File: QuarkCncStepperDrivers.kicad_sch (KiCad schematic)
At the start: 2 parts, among them J1 Conn_01x14, J2 Conn_01x14

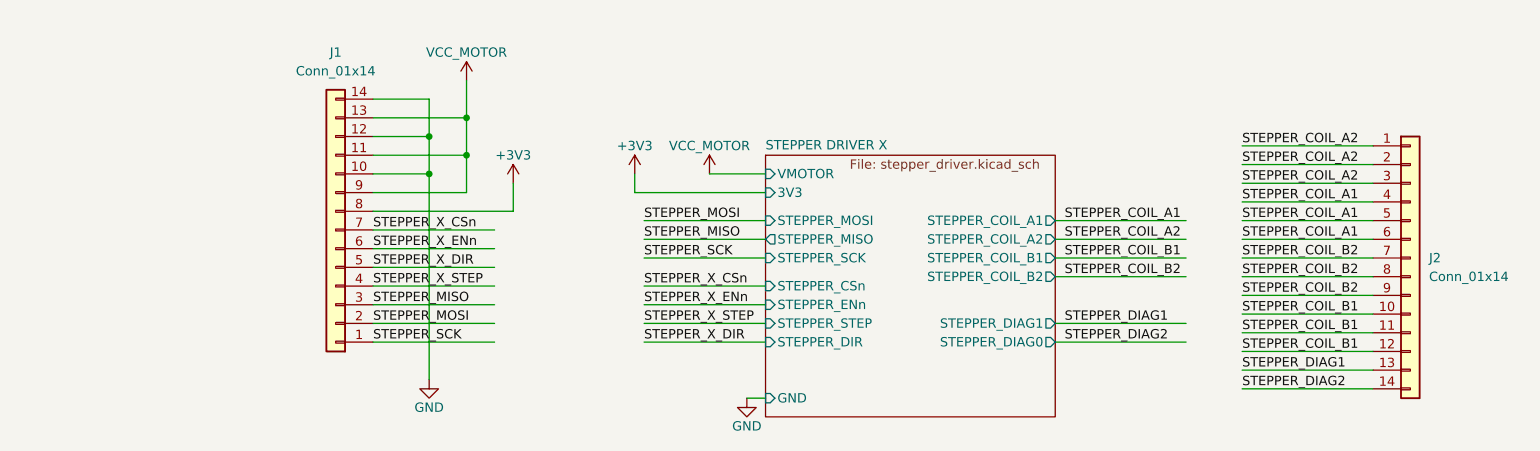
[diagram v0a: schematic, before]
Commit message: Removed caps from board. Will be placed on main board
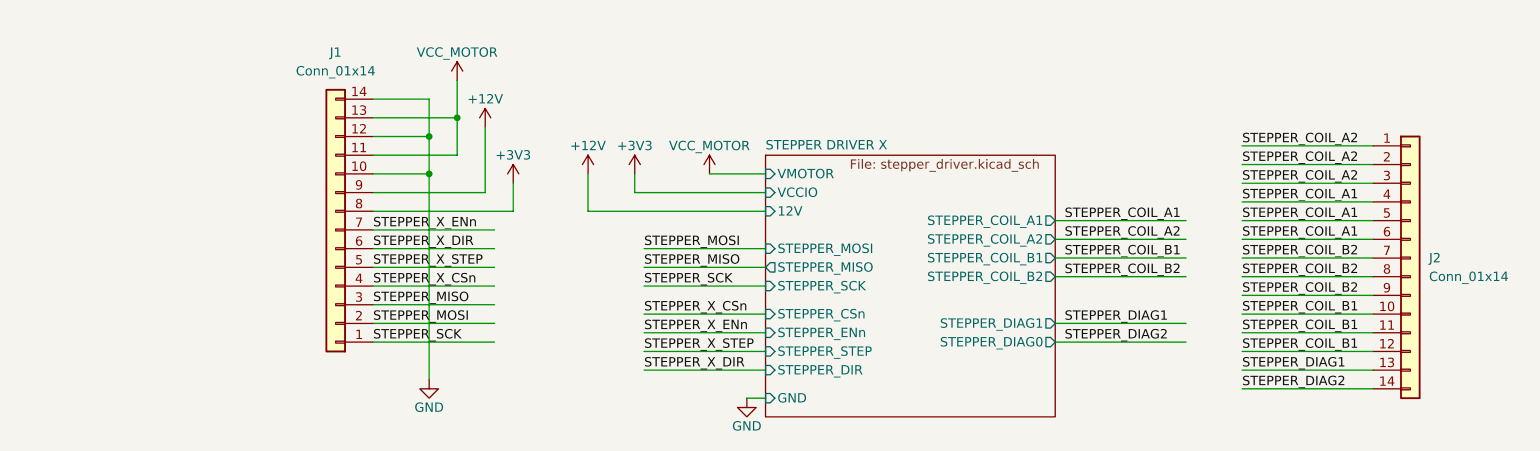
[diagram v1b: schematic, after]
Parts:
- J1, J2: LCSC (none) -> C2894937
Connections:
- net STEPPER_X_CSn: now also J1.4 (Pin_4); no longer J1.7 (Pin_7)
- net STEPPER_X_DIR: now also J1.6 (Pin_6); no longer J1.5 (Pin_5)
- net STEPPER_X_ENn: now also J1.7 (Pin_7); no longer J1.6 (Pin_6)
- net STEPPER_X_STEP: now also J1.5 (Pin_5); no longer J1.4 (Pin_4)
- net VCC: no longer J1.9 (Pin_9)
- new net +12V: J1.9 (Pin_9)
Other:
- sheet STEPPER DRIVER X ports: added 12V, VCCIO; removed 3V3

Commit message: triple connector
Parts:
- removed J1: Conn_01x14, Connector_PinHeader_2.54mm:PinHeader_1x14_P2.54mm_Vertical, symbol Connector_Generic:Conn_01x14
- added J1: (no value), symbol Connector_Generic:Conn_02x03_Odd_Even
- added J2: Conn_01x08, Connector_PinSocket_2.54mm:PinSocket_1x08_P2.54mm_Vertical, symbol Connector_Generic:Conn_01x08
- renumbered J2 to J3
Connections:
- net +12V: now also J1.2 (Pin_2)
- net +3V3: now also J1.1 (Pin_1)
- net GND: now also J1.3 (Pin_3), J1.4 (Pin_4), J2.5 (Pin_5)
- net STEPPER_MISO: now also J2.3 (Pin_3)
- net STEPPER_MOSI: now also J2.2 (Pin_2)
- net STEPPER_SCK: now also J2.1 (Pin_1)
- net STEPPER_X_CSn: now also J2.4 (Pin_4)
- net STEPPER_X_DIR: now also J2.7 (Pin_7)
- net STEPPER_X_ENn: now also J2.8 (Pin_8)
- net STEPPER_X_STEP: now also J2.6 (Pin_6)
- net VCC: now also J1.5 (Pin_5), J1.6 (Pin_6)
